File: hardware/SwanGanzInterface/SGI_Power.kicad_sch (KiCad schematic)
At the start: 23 parts, among them J1 2479774-1, Q1 SQ2389CES-T1_GE3, SW1 Power_Switch, U1 LM2937ET-3.3_NOPB, U2 LM4041CILPR, U3 OPA2350

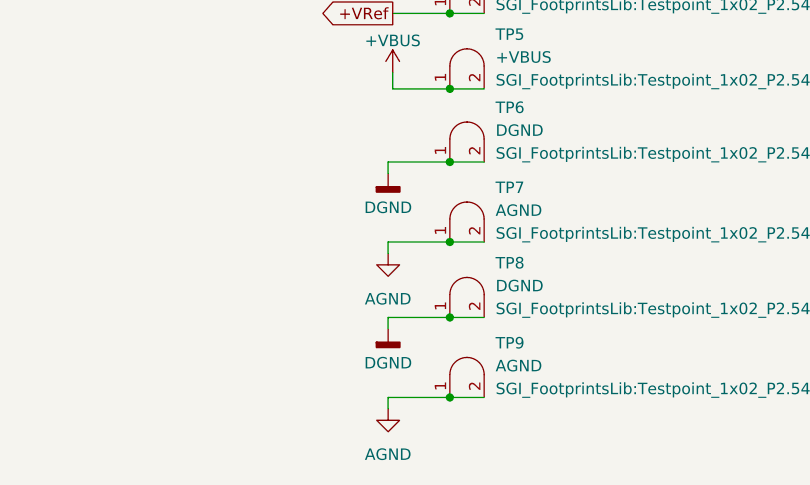
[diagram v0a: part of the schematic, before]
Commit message: Consolidated Grounds
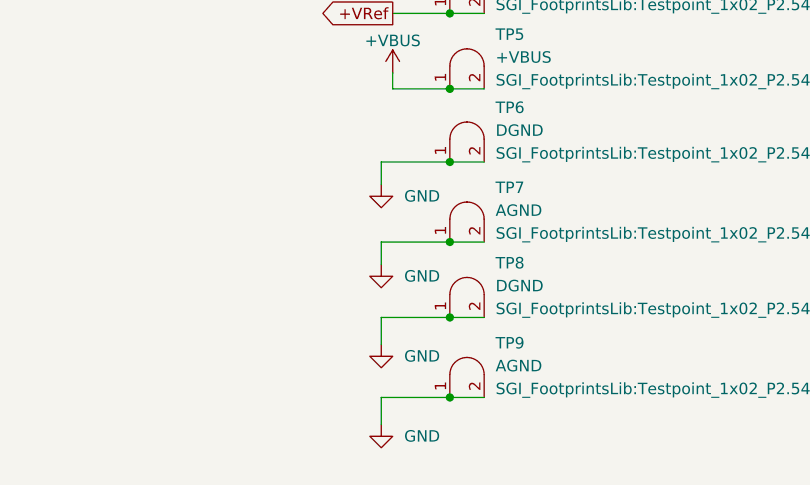
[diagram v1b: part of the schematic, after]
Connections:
- net AGND is gone; now on net GND: TP7.1 (A), TP7.2 (B), TP9.1 (A), TP9.2 (B)
- net DGND is gone; now on net GND: TP6.1 (A), TP6.2 (B), TP8.1 (A), TP8.2 (B)

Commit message: Started Layout
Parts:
- removed TP3: +3V3A, SGI_FootprintsLib:Testpoint_1x02_P2.54mm, symbol SGI_SymbolLib:Testpoint
- removed TP8: DGND, SGI_FootprintsLib:Testpoint_1x02_P2.54mm, symbol SGI_SymbolLib:Testpoint
- removed TP9: AGND, SGI_FootprintsLib:Testpoint_1x02_P2.54mm, symbol SGI_SymbolLib:Testpoint
- TP2: value +3V3D -> +3V3
- TP6: value DGND -> GND
- TP7: value AGND -> GND
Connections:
- net +3V3D is gone; now on net +3V3: TP2.1 (A), TP2.2 (B)

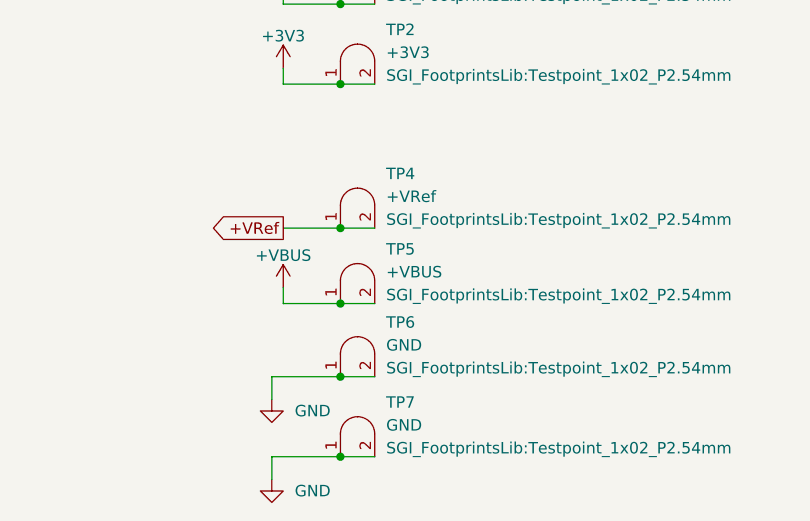
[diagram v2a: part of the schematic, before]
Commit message: Reannotated symbols
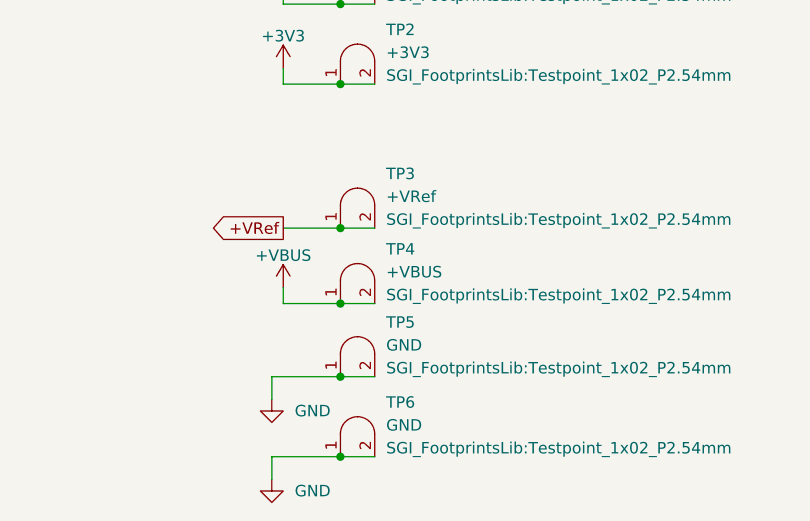
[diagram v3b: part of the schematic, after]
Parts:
- renumbered TP4 to TP3, TP5 to TP4, TP6 to TP5, TP7 to TP6
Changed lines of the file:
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@@
 		(on_board yes)
 		(dnp no)
-		(property "Reference" "#PWR015"
+		(property "Reference" "#PWR013"
 			(at 224.79 88.9 0)
 			(effects
@@
 			(project "SwanGanzInterface"
 				(path "/4e9a6e30-f660-472b-9696-bea1f34b4545/090a1e64-9482-4912-b352-6eea35714559"
-					(reference "#PWR015")
+					(reference "#PWR013")
 					(unit 1)
 				)
@@
 		(dnp no)
 		(fields_autoplaced yes)
-		(property "Reference" "TP5"
+		(property "Reference" "TP4"
 			(at 236.22 105.2193 0)
 			(effects
@@
 			(project "SwanGanzInterface"
 				(path "/4e9a6e30-f660-472b-9696-bea1f34b4545/090a1e64-9482-4912-b352-6eea35714559"
-					(reference "TP5")
+					(reference "TP4")
 					(unit 1)
 				)
@@
 		(dnp no)
 		(fields_autoplaced yes)
-		(property "Reference" "TP7"
+		(property "Reference" "TP6"
 			(at 236.22 122.2373 0)
 			(effects
@@
 			(project "SwanGanzInterface"
 				(path "/4e9a6e30-f660-472b-9696-bea1f34b4545/090a1e64-9482-4912-b352-6eea35714559"
-					(reference "TP7")
+					(reference "TP6")
 					(unit 1)
 				)
@@
 		(on_board yes)
 		(dnp no)
-		(property "Reference" "#PWR017"
+		(property "Reference" "#PWR014"
 			(at 224.79 113.284 0)
 			(effects
@@
 			(project "SwanGanzInterface"
 				(path "/4e9a6e30-f660-472b-9696-bea1f34b4545/090a1e64-9482-4912-b352-6eea35714559"
-					(reference "#PWR017")
+					(reference "#PWR014")
 					(unit 1)
 				)
@@
 		(on_board yes)
 		(dnp no)
-		(property "Reference" "#PWR014"
+		(property "Reference" "#PWR012"
 			(at 224.79 80.01 0)
 			(effects
@@
 			(project "SwanGanzInterface"
 				(path "/4e9a6e30-f660-472b-9696-bea1f34b4545/090a1e64-9482-4912-b352-6eea35714559"
-					(reference "#PWR014")
+					(reference "#PWR012")
 					(unit 1)
 				)
@@
 		(dnp no)
 		(fields_autoplaced yes)
-		(property "Reference" "TP4"
+		(property "Reference" "TP3"
 			(at 236.22 96.8373 0)
 			(effects
@@
 			(project "SwanGanzInterface"
 				(path "/4e9a6e30-f660-472b-9696-bea1f34b4545/090a1e64-9482-4912-b352-6eea35714559"
-					(reference "TP4")
+					(reference "TP3")
 					(unit 1)
 				)
@@
 		(on_board yes)
 		(dnp no)
-		(property "Reference" "#PWR018"
+		(property "Reference" "#PWR015"
 			(at 267.462 33.782 0)
 			(effects
@@
 			(project "SwanGanzInterface"
 				(path "/4e9a6e30-f660-472b-9696-bea1f34b4545/090a1e64-9482-4912-b352-6eea35714559"
-					(reference "#PWR018")
+					(reference "#PWR015")
 					(unit 1)
 				)
@@
 		(dnp no)
 		(fields_autoplaced yes)
-		(property "Reference" "#PWR019"
+		(property "Reference" "#PWR016"
 			(at 267.462 64.262 0)
 			(effects
@@
 			(project "SwanGanzInterface"
 				(path "/4e9a6e30-f660-472b-9696-bea1f34b4545/090a1e64-9482-4912-b352-6eea35714559"
-					(reference "#PWR019")
+					(reference "#PWR016")
 					(unit 1)
 				)
@@
 		(dnp no)
 		(fields_autoplaced yes)
-		(property "Reference" "TP6"
+		(property "Reference" "TP5"
 			(at 236.22 113.3473 0)
 			(effects
@@
 			(project "SwanGanzInterface"
 				(path "/4e9a6e30-f660-472b-9696-bea1f34b4545/090a1e64-9482-4912-b352-6eea35714559"
-					(reference "TP6")
-					(unit 1)
-				)
+					(reference "TP5")
+					(unit 1)
+				)
